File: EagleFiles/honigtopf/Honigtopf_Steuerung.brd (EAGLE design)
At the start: 71.1 x 58.4 mm, 11 parts

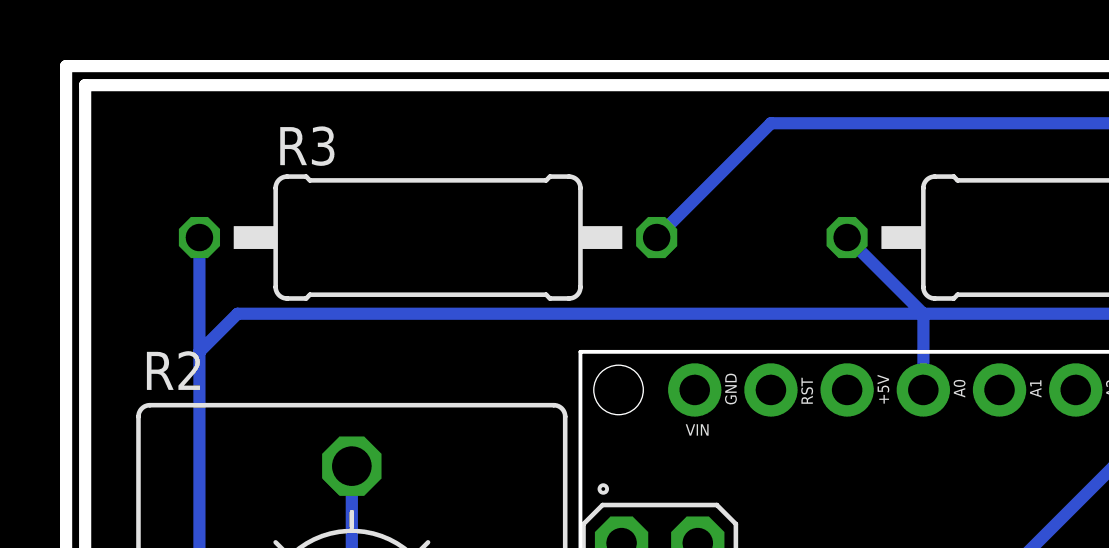
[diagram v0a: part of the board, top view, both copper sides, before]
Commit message: added supply pins
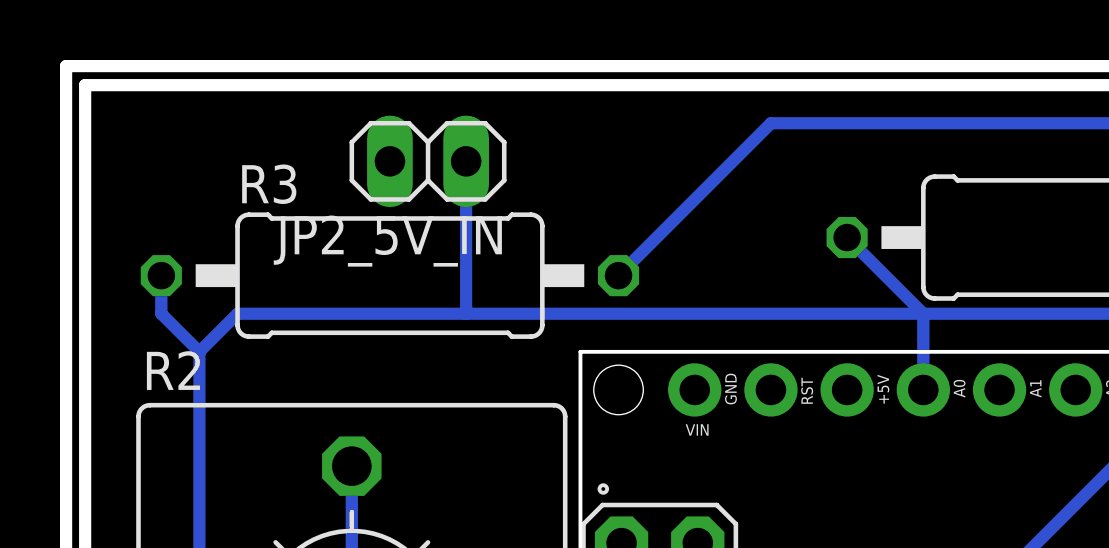
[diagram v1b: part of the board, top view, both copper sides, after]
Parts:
- added JP2_5V_IN: (no value), pinhead:1X02
- moved R3 1.80 mm to (8.89, 73.7)
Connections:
- net 5V: now also JP2_5V_IN.1
- net GND: now also JP2_5V_IN.2
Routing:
- net 5V: track 95.6 -> 99.9 mm
- net N$2: track 74.1 -> 75.9 mm
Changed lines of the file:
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@@
 <?xml version="1.0" encoding="utf-8"?>
 <!DOCTYPE eagle SYSTEM "eagle.dtd">
-<eagle version="8.1.0">
+<eagle version="7.6.0">
 <drawing>
 <settings>
@@
 <element name="R1" library="resistor" package="0411/15" value="4,7k" x="31.75" y="74.93" rot="R180"/>
 <element name="R2" library="pot" package="CA14V" value="10k" x="7.62" y="62.23"/>
-<element name="R3" library="resistor" package="0411/15" value="220" x="10.16" y="74.93"/>
+<element name="R3" library="resistor" package="0411/15" value="220" x="8.89" y="73.66"/>
 <element name="S1_UP" library="switch-omron" package="B3F-10XX" value="" x="7.62" y="39.37">
 <attribute name="MF" value="" x="7.62" y="39.37" size="1.778" layer="27" display="off"/>
@@
 <element name="H1" library="holes" package="3,2" value="MOUNT-HOLE3.2" x="2.54" y="47.625"/>
 <element name="H2" library="holes" package="3,2" value="MOUNT-HOLE3.2" x="64.77" y="74.93"/>
+<element name="JP2_5V_IN" library="pinhead" package="1X02" value="" x="10.16" y="77.47" rot="R180"/>
 </elements>
 <signals>
@@
 <wire x1="10.16" y1="54.61" x2="10.16" y2="48.26" width="0.4064" layer="1"/>
 <via x="10.16" y="48.26" extent="1-16" drill="0.6" shape="square"/>
+<contactref element="JP2_5V_IN" pad="2"/>
 </signal>
 <signal name="5V">
@@
 <contactref element="DIS1" pad="2"/>
 <contactref element="R3" pad="1"/>
-<wire x1="2.54" y1="74.93" x2="2.54" y2="71.12" width="0.4064" layer="16"/>
 <wire x1="2.54" y1="71.12" x2="2.54" y2="54.61" width="0.4064" layer="16"/>
 <wire x1="2.54" y1="54.61" x2="7.62" y2="49.53" width="0.4064" layer="16"/>
@@
 <wire x1="26.67" y1="72.39" x2="24.13" y2="74.93" width="0.4064" layer="16"/>
 <wire x1="26.67" y1="69.85" x2="26.67" y2="72.39" width="0.4064" layer="16"/>
-<wire x1="26.67" y1="72.39" x2="3.81" y2="72.39" width="0.4064" layer="16"/>
+<wire x1="26.67" y1="72.39" x2="11.43" y2="72.39" width="0.4064" layer="16"/>
+<wire x1="11.43" y1="72.39" x2="3.81" y2="72.39" width="0.4064" layer="16"/>
 <wire x1="3.81" y1="72.39" x2="2.54" y2="71.12" width="0.4064" layer="16"/>
+<contactref element="JP2_5V_IN" pad="1"/>
+<wire x1="1.27" y1="73.66" x2="1.27" y2="72.39" width="0.4064" layer="16"/>
+<wire x1="1.27" y1="72.39" x2="2.54" y2="71.12" width="0.4064" layer="16"/>
+<wire x1="11.43" y1="77.47" x2="11.43" y2="72.39" width="0.4064" layer="16"/>
 </signal>
 <signal name="N$4">
@@
 <contactref element="DIS1" pad="15"/>
 <contactref element="R3" pad="2"/>
-<wire x1="17.78" y1="74.93" x2="21.59" y2="78.74" width="0.4064" layer="16"/>
+<wire x1="16.51" y1="73.66" x2="21.59" y2="78.74" width="0.4064" layer="16"/>
 <wire x1="21.59" y1="78.74" x2="57.15" y2="78.74" width="0.4064" layer="16"/>
 <wire x1="57.15" y1="78.74" x2="59.69" y2="76.2" width="0.4064" layer="16"/>
